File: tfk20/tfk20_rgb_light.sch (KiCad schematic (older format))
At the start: 0 parts

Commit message: Continue on tfk20
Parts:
- added C? (x4): 104, symbol Device:C_Small
- added D? (x4): WS2812B, LED_SMD:LED_WS2812B_PLCC4_5.0x5.0mm_P3.2mm, symbol LED:WS2812B
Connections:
- net RGB_LIGHT: now also D?.4 (DIN)
- new net: D?.2 (DOUT), D?.4 (DIN) (x3)
- new net +5V: C?.1, C?.1, C?.1, C?.1, D?.1 (VDD), D?.1 (VDD), D?.1 (VDD), D?.1 (VDD)
- new net GND: C?.2, C?.2, C?.2, C?.2, D?.3 (VSS), D?.3 (VSS), D?.3 (VSS), D?.3 (VSS)
- no-connect marks 0 -> 2

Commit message: RGB LED driver
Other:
- note added: "RGB underglow LEDs"
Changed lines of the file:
@@
 $Descr A4 11693 8268
 encoding utf-8
-Sheet 4 4
+Sheet 3 4
 Title "tfk20"
 Date "2021-02-02"
@@
 P 2250 1550
 AR Path="/602C3063/601B5D10" Ref="#PWR?"  Part="1"
-AR Path="/602C340B/601B5D10" Ref="#PWR?"  Part="1"
-F 0 "#PWR?" H 2250 1300 50  0001 C CNN
+AR Path="/602C340B/601B5D10" Ref="#PWR0181"  Part="1"
+F 0 "#PWR0181" H 2250 1300 50  0001 C CNN
 F 1 "GND" H 2255 1377 50  0000 C CNN
 F 2 "" H 2250 1550 50  0001 C CNN
@@
 P 1850 1200
 AR Path="/602C3063/601B5D16" Ref="#PWR?"  Part="1"
-AR Path="/602C340B/601B5D16" Ref="#PWR?"  Part="1"
-F 0 "#PWR?" H 1850 1050 50  0001 C CNN
+AR Path="/602C340B/601B5D16" Ref="#PWR0182"  Part="1"
+F 0 "#PWR0182" H 1850 1050 50  0001 C CNN
 F 1 "+5V" H 1865 1373 50  0000 C CNN
 F 2 "" H 1850 1200 50  0001 C CNN
@@
 P 1850 2150
 AR Path="/602C3063/601B5D1E" Ref="#PWR?"  Part="1"
-AR Path="/602C340B/601B5D1E" Ref="#PWR?"  Part="1"
-F 0 "#PWR?" H 1850 1900 50  0001 C CNN
+AR Path="/602C340B/601B5D1E" Ref="#PWR0183"  Part="1"
+F 0 "#PWR0183" H 1850 1900 50  0001 C CNN
 F 1 "GND" H 1855 1977 50  0000 C CNN
 F 2 "" H 1850 2150 50  0001 C CNN
@@
 P 3600 1500
 AR Path="/602C3063/601B5D32" Ref="#PWR?"  Part="1"
-AR Path="/602C340B/601B5D32" Ref="#PWR?"  Part="1"
-F 0 "#PWR?" H 3600 1250 50  0001 C CNN
+AR Path="/602C340B/601B5D32" Ref="#PWR0184"  Part="1"
+F 0 "#PWR0184" H 3600 1250 50  0001 C CNN
 F 1 "GND" H 3605 1327 50  0000 C CNN
 F 2 "" H 3600 1500 50  0001 C CNN
@@
 P 3150 1200
 AR Path="/602C3063/601B5D38" Ref="#PWR?"  Part="1"
-AR Path="/602C340B/601B5D38" Ref="#PWR?"  Part="1"
-F 0 "#PWR?" H 3150 1050 50  0001 C CNN
+AR Path="/602C340B/601B5D38" Ref="#PWR0185"  Part="1"
+F 0 "#PWR0185" H 3150 1050 50  0001 C CNN
 F 1 "+5V" H 3165 1373 50  0000 C CNN
 F 2 "" H 3150 1200 50  0001 C CNN
@@
 P 3150 2150
 AR Path="/602C3063/601B5D40" Ref="#PWR?"  Part="1"
-AR Path="/602C340B/601B5D40" Ref="#PWR?"  Part="1"
-F 0 "#PWR?" H 3150 1900 50  0001 C CNN
+AR Path="/602C340B/601B5D40" Ref="#PWR0186"  Part="1"
+F 0 "#PWR0186" H 3150 1900 50  0001 C CNN
 F 1 "GND" H 3155 1977 50  0000 C CNN
 F 2 "" H 3150 2150 50  0001 C CNN
@@
 P 4850 1550
 AR Path="/602C3063/601B5D55" Ref="#PWR?"  Part="1"
-AR Path="/602C340B/601B5D55" Ref="#PWR?"  Part="1"
-F 0 "#PWR?" H 4850 1300 50  0001 C CNN
+AR Path="/602C340B/601B5D55" Ref="#PWR0187"  Part="1"
+F 0 "#PWR0187" H 4850 1300 50  0001 C CNN
 F 1 "GND" H 4855 1377 50  0000 C CNN
 F 2 "" H 4850 1550 50  0001 C CNN
@@
 P 4450 1200
 AR Path="/602C3063/601B5D5B" Ref="#PWR?"  Part="1"
-AR Path="/602C340B/601B5D5B" Ref="#PWR?"  Part="1"
-F 0 "#PWR?" H 4450 1050 50  0001 C CNN
+AR Path="/602C340B/601B5D5B" Ref="#PWR0188"  Part="1"
+F 0 "#PWR0188" H 4450 1050 50  0001 C CNN
 F 1 "+5V" H 4465 1373 50  0000 C CNN
 F 2 "" H 4450 1200 50  0001 C CNN
@@
 P 4450 2150
 AR Path="/602C3063/601B5D63" Ref="#PWR?"  Part="1"
-AR Path="/602C340B/601B5D63" Ref="#PWR?"  Part="1"
-F 0 "#PWR?" H 4450 1900 50  0001 C CNN
+AR Path="/602C340B/601B5D63" Ref="#PWR0189"  Part="1"
+F 0 "#PWR0189" H 4450 1900 50  0001 C CNN
 F 1 "GND" H 4455 1977 50  0000 C CNN
 F 2 "" H 4450 2150 50  0001 C CNN
@@
 P 6200 1500
 AR Path="/602C3063/601B5D77" Ref="#PWR?"  Part="1"
-AR Path="/602C340B/601B5D77" Ref="#PWR?"  Part="1"
-F 0 "#PWR?" H 6200 1250 50  0001 C CNN
+AR Path="/602C340B/601B5D77" Ref="#PWR0190"  Part="1"
+F 0 "#PWR0190" H 6200 1250 50  0001 C CNN
 F 1 "GND" H 6205 1327 50  0000 C CNN
 F 2 "" H 6200 1500 50  0001 C CNN
@@
 P 5750 1200
 AR Path="/602C3063/601B5D7D" Ref="#PWR?"  Part="1"
-AR Path="/602C340B/601B5D7D" Ref="#PWR?"  Part="1"
-F 0 "#PWR?" H 5750 1050 50  0001 C CNN
+AR Path="/602C340B/601B5D7D" Ref="#PWR0191"  Part="1"
+F 0 "#PWR0191" H 5750 1050 50  0001 C CNN
 F 1 "+5V" H 5765 1373 50  0000 C CNN
 F 2 "" H 5750 1200 50  0001 C CNN
@@
 P 5750 2150
 AR Path="/602C3063/601B5D85" Ref="#PWR?"  Part="1"
-AR Path="/602C340B/601B5D85" Ref="#PWR?"  Part="1"
-F 0 "#PWR?" H 5750 1900 50  0001 C CNN
+AR Path="/602C340B/601B5D85" Ref="#PWR0192"  Part="1"
+F 0 "#PWR0192" H 5750 1900 50  0001 C CNN
 F 1 "GND" H 5755 1977 50  0000 C CNN
 F 2 "" H 5750 2150 50  0001 C CNN
@@
 NoConn ~ 6100 1850
 NoConn ~ -2800 -100
+Text Notes 750  850  0    50   ~ 0
+RGB underglow LEDs
+Wire Notes Line
+	700  700  6650 700
+Wire Notes Line
+	6650 700  6650 2500
+Wire Notes Line
+	6650 2500 700  2500
+Wire Notes Line
+	700  2500 700  700
 $EndSCHEMATC

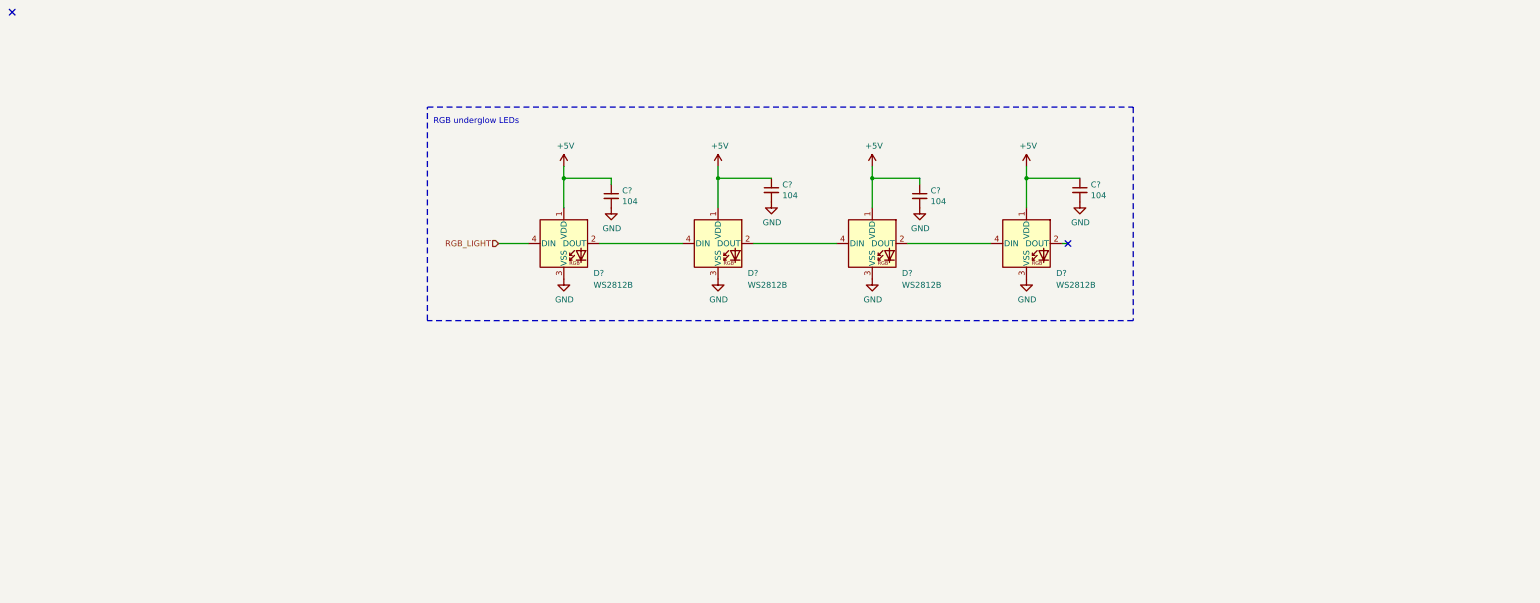
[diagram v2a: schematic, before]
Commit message: Change MCU, add another row, add reset button
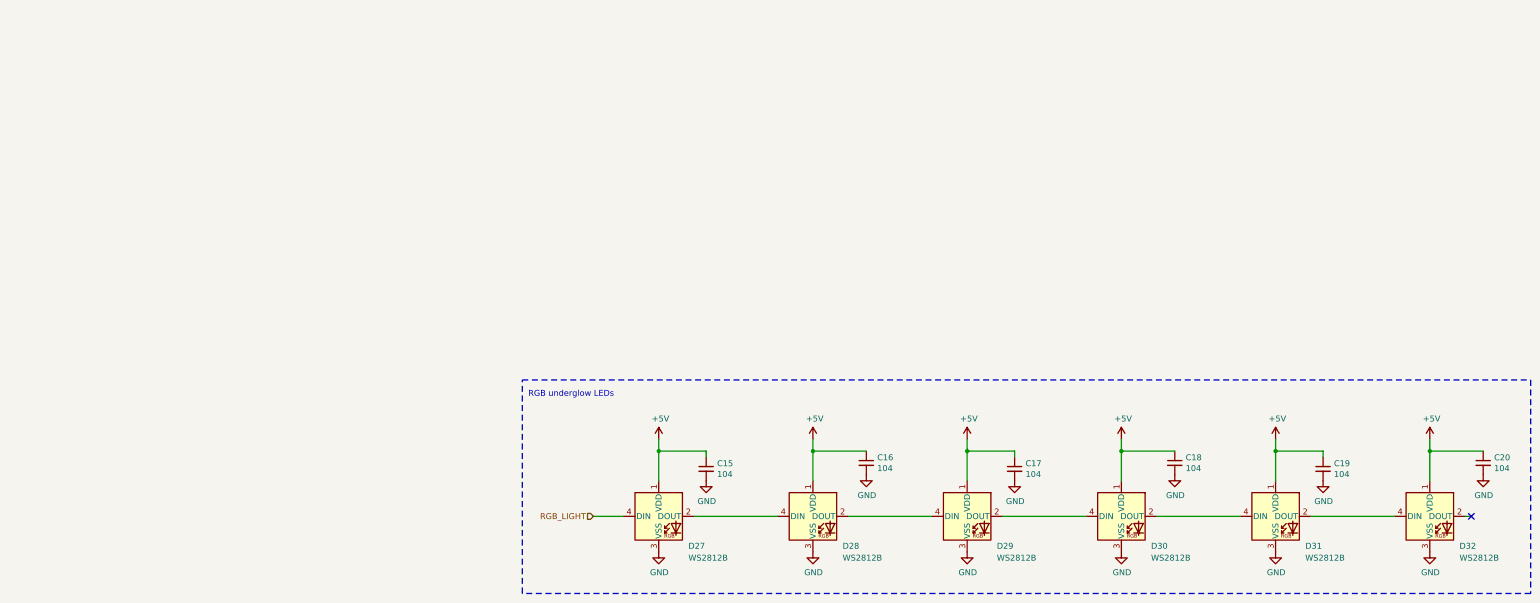
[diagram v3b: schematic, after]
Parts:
- added C19, C20: 104, symbol Device:C_Small
- added D31, D32: WS2812B, LED_SMD:LED_WS2812B_PLCC4_5.0x5.0mm_P3.2mm, symbol LED:WS2812B
- gave numbers to parts that had none: 8
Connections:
- net +5V: now also C19.1, C20.1, D31.1 (VDD), D32.1 (VDD)
- net GND: now also C19.2, C20.2, D31.3 (VSS), D32.3 (VSS)
- net at D30.2 (DOUT): now also D31.4 (DIN)
- new net: D31.2 (DOUT), D32.4 (DIN)
- no-connect marks 2 -> 1
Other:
- moved on the sheet: C15, C16, C17, C18, D27, D28, D29, D30

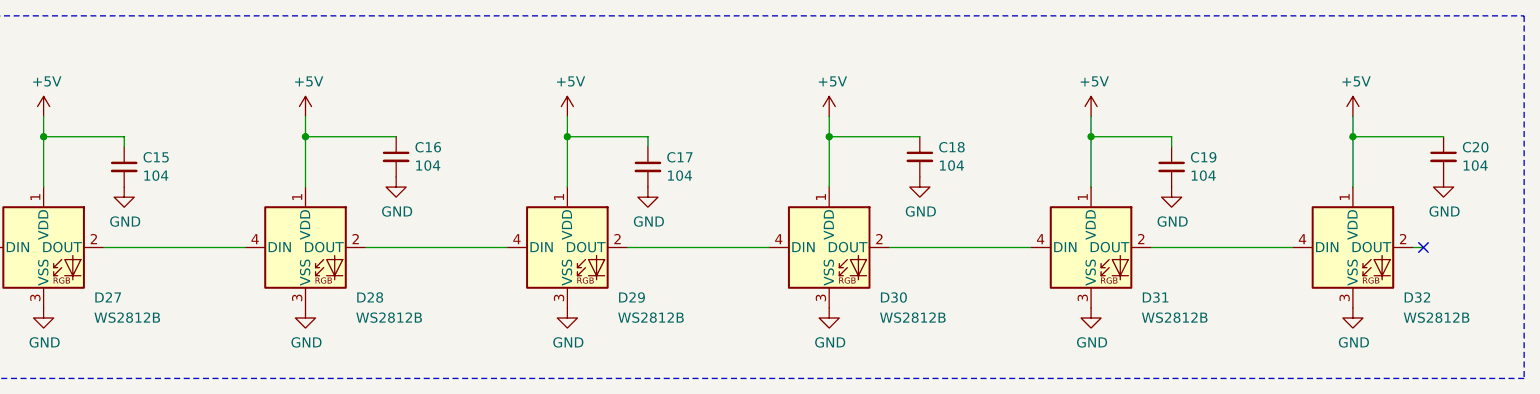
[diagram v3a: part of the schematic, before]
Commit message: Implement sophisticated USB-C protection
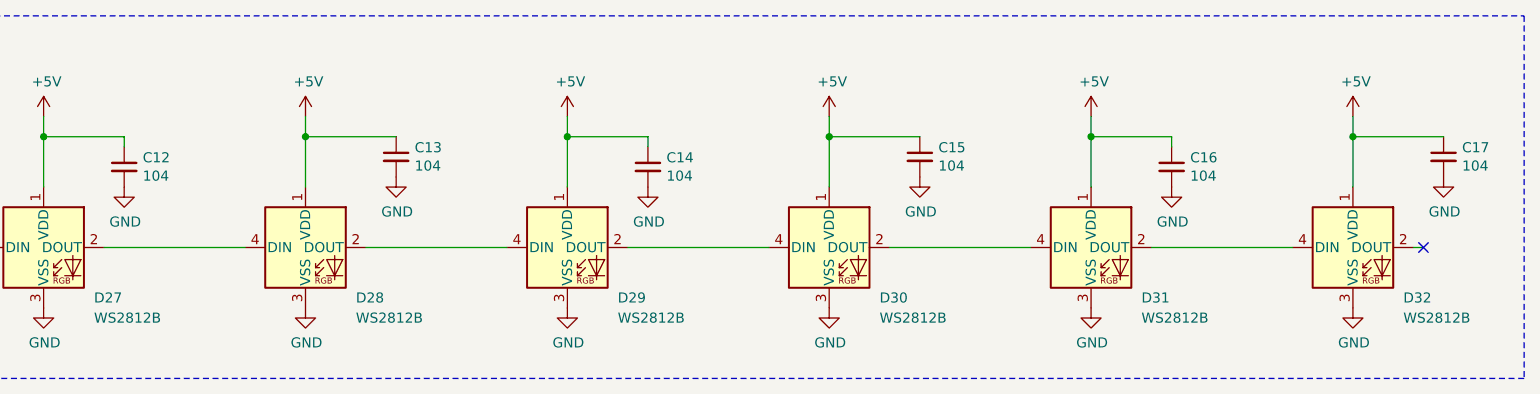
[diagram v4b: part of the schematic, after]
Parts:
- renumbered C15 to C12, C16 to C13, C17 to C14, C18 to C15, C19 to C16, C20 to C17
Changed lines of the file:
@@
 $Descr A4 11693 8268
 encoding utf-8
-Sheet 3 4
+Sheet 3 5
 Title "tfk20"
 Date "2021-02-02"
@@
 P 3050 3750
 AR Path="/602C3063/601B5D07" Ref="C?"  Part="1"
-AR Path="/602C340B/601B5D07" Ref="C15"  Part="1"
-F 0 "C15" H 3142 3796 50  0000 L CNN
+AR Path="/602C340B/601B5D07" Ref="C12"  Part="1"
+F 0 "C12" H 3142 3796 50  0000 L CNN
 F 1 "104" H 3142 3705 50  0000 L CNN
 F 2 "" H 3050 3750 50  0001 C CNN
@@
 P 3050 3850
 AR Path="/602C3063/601B5D10" Ref="#PWR?"  Part="1"
-AR Path="/602C340B/601B5D10" Ref="#PWR034"  Part="1"
-F 0 "#PWR034" H 3050 3600 50  0001 C CNN
+AR Path="/602C340B/601B5D10" Ref="#PWR022"  Part="1"
+F 0 "#PWR022" H 3050 3600 50  0001 C CNN
 F 1 "GND" H 3055 3677 50  0000 C CNN
 F 2 "" H 3050 3850 50  0001 C CNN
@@
 P 2650 3500
 AR Path="/602C3063/601B5D16" Ref="#PWR?"  Part="1"
-AR Path="/602C340B/601B5D16" Ref="#PWR032"  Part="1"
-F 0 "#PWR032" H 2650 3350 50  0001 C CNN
+AR Path="/602C340B/601B5D16" Ref="#PWR020"  Part="1"
+F 0 "#PWR020" H 2650 3350 50  0001 C CNN
 F 1 "+5V" H 2665 3673 50  0000 C CNN
 F 2 "" H 2650 3500 50  0001 C CNN
@@
 P 4400 3700
 AR Path="/602C3063/601B5D2A" Ref="C?"  Part="1"
-AR Path="/602C340B/601B5D2A" Ref="C16"  Part="1"
-F 0 "C16" H 4492 3746 50  0000 L CNN
+AR Path="/602C340B/601B5D2A" Ref="C13"  Part="1"
+F 0 "C13" H 4492 3746 50  0000 L CNN
 F 1 "104" H 4492 3655 50  0000 L CNN
 F 2 "" H 4400 3700 50  0001 C CNN
@@
 P 4400 3800
 AR Path="/602C3063/601B5D32" Ref="#PWR?"  Part="1"
-AR Path="/602C340B/601B5D32" Ref="#PWR037"  Part="1"
-F 0 "#PWR037" H 4400 3550 50  0001 C CNN
+AR Path="/602C340B/601B5D32" Ref="#PWR025"  Part="1"
+F 0 "#PWR025" H 4400 3550 50  0001 C CNN
 F 1 "GND" H 4405 3627 50  0000 C CNN
 F 2 "" H 4400 3800 50  0001 C CNN
@@
 P 3950 3500
 AR Path="/602C3063/601B5D38" Ref="#PWR?"  Part="1"
-AR Path="/602C340B/601B5D38" Ref="#PWR035"  Part="1"
-F 0 "#PWR035" H 3950 3350 50  0001 C CNN
+AR Path="/602C340B/601B5D38" Ref="#PWR023"  Part="1"
+F 0 "#PWR023" H 3950 3350 50  0001 C CNN
 F 1 "+5V" H 3965 3673 50  0000 C CNN
 F 2 "" H 3950 3500 50  0001 C CNN
@@
 P 3950 4450
 AR Path="/602C3063/601B5D40" Ref="#PWR?"  Part="1"
-AR Path="/602C340B/601B5D40" Ref="#PWR036"  Part="1"
-F 0 "#PWR036" H 3950 4200 50  0001 C CNN
+AR Path="/602C340B/601B5D40" Ref="#PWR024"  Part="1"
+F 0 "#PWR024" H 3950 4200 50  0001 C CNN
 F 1 "GND" H 3955 4277 50  0000 C CNN
 F 2 "" H 3950 4450 50  0001 C CNN
@@
 P 5650 3750
 AR Path="/602C3063/601B5D4C" Ref="C?"  Part="1"
-AR Path="/602C340B/601B5D4C" Ref="C17"  Part="1"
-F 0 "C17" H 5742 3796 50  0000 L CNN
+AR Path="/602C340B/601B5D4C" Ref="C14"  Part="1"
+F 0 "C14" H 5742 3796 50  0000 L CNN
 F 1 "104" H 5742 3705 50  0000 L CNN
 F 2 "" H 5650 3750 50  0001 C CNN
@@
 P 5650 3850
 AR Path="/602C3063/601B5D55" Ref="#PWR?"  Part="1"
-AR Path="/602C340B/601B5D55" Ref="#PWR040"  Part="1"
-F 0 "#PWR040" H 5650 3600 50  0001 C CNN
+AR Path="/602C340B/601B5D55" Ref="#PWR028"  Part="1"
+F 0 "#PWR028" H 5650 3600 50  0001 C CNN
 F 1 "GND" H 5655 3677 50  0000 C CNN
 F 2 "" H 5650 3850 50  0001 C CNN
@@
 P 5250 3500
 AR Path="/602C3063/601B5D5B" Ref="#PWR?"  Part="1"
-AR Path="/602C340B/601B5D5B" Ref="#PWR038"  Part="1"
-F 0 "#PWR038" H 5250 3350 50  0001 C CNN
+AR Path="/602C340B/601B5D5B" Ref="#PWR026"  Part="1"
+F 0 "#PWR026" H 5250 3350 50  0001 C CNN
 F 1 "+5V" H 5265 3673 50  0000 C CNN
 F 2 "" H 5250 3500 50  0001 C CNN
@@
 P 5250 4450
 AR Path="/602C3063/601B5D63" Ref="#PWR?"  Part="1"
-AR Path="/602C340B/601B5D63" Ref="#PWR039"  Part="1"
-F 0 "#PWR039" H 5250 4200 50  0001 C CNN
+AR Path="/602C340B/601B5D63" Ref="#PWR027"  Part="1"
+F 0 "#PWR027" H 5250 4200 50  0001 C CNN
 F 1 "GND" H 5255 4277 50  0000 C CNN
 F 2 "" H 5250 4450 50  0001 C CNN
@@
 P 7000 3700
 AR Path="/602C3063/601B5D6F" Ref="C?"  Part="1"
-AR Path="/602C340B/601B5D6F" Ref="C18"  Part="1"
-F 0 "C18" H 7092 3746 50  0000 L CNN
+AR Path="/602C340B/601B5D6F" Ref="C15"  Part="1"
+F 0 "C15" H 7092 3746 50  0000 L CNN
 F 1 "104" H 7092 3655 50  0000 L CNN
 F 2 "" H 7000 3700 50  0001 C CNN
@@
 P 7000 3800
 AR Path="/602C3063/601B5D77" Ref="#PWR?"  Part="1"
-AR Path="/602C340B/601B5D77" Ref="#PWR043"  Part="1"
-F 0 "#PWR043" H 7000 3550 50  0001 C CNN
+AR Path="/602C340B/601B5D77" Ref="#PWR031"  Part="1"
+F 0 "#PWR031" H 7000 3550 50  0001 C CNN
 F 1 "GND" H 7005 3627 50  0000 C CNN
 F 2 "" H 7000 3800 50  0001 C CNN
@@
 P 6550 3500
 AR Path="/602C3063/601B5D7D" Ref="#PWR?"  Part="1"
-AR Path="/602C340B/601B5D7D" Ref="#PWR041"  Part="1"
-F 0 "#PWR041" H 6550 3350 50  0001 C CNN
+AR Path="/602C340B/601B5D7D" Ref="#PWR029"  Part="1"
+F 0 "#PWR029" H 6550 3350 50  0001 C CNN
 F 1 "+5V" H 6565 3673 50  0000 C CNN
 F 2 "" H 6550 3500 50  0001 C CNN
@@
 P 6550 4450
 AR Path="/602C3063/601B5D85" Ref="#PWR?"  Part="1"
-AR Path="/602C340B/601B5D85" Ref="#PWR042"  Part="1"
-F 0 "#PWR042" H 6550 4200 50  0001 C CNN
+AR Path="/602C340B/601B5D85" Ref="#PWR030"  Part="1"
+F 0 "#PWR030" H 6550 4200 50  0001 C CNN
 F 1 "GND" H 6555 4277 50  0000 C CNN
 F 2 "" H 6550 4450 50  0001 C CNN
@@
 	1500 4800 1500 3000
 $Comp
-L power:GND #PWR033
+L power:GND #PWR021
 U 1 1 606DE53F
 P 2650 4450
-F 0 "#PWR033" H 2650 4200 50  0001 C CNN
+F 0 "#PWR021" H 2650 4200 50  0001 C CNN
 F 1 "GND" H 2655 4277 50  0000 C CNN
 F 2 "" H 2650 4450 50  0001 C CNN
@@
 P 8250 3750
 AR Path="/602C3063/60DF2224" Ref="C?"  Part="1"
-AR Path="/602C340B/60DF2224" Ref="C19"  Part="1"
-F 0 "C19" H 8342 3796 50  0000 L CNN
+AR Path="/602C340B/60DF2224" Ref="C16"  Part="1"
+F 0 "C16" H 8342 3796 50  0000 L CNN
 F 1 "104" H 8342 3705 50  0000 L CNN
 F 2 "" H 8250 3750 50  0001 C CNN
@@
 P 8250 3850
 AR Path="/602C3063/60DF222D" Ref="#PWR?"  Part="1"
-AR Path="/602C340B/60DF222D" Ref="#PWR046"  Part="1"
-F 0 "#PWR046" H 8250 3600 50  0001 C CNN
+AR Path="/602C340B/60DF222D" Ref="#PWR034"  Part="1"
+F 0 "#PWR034" H 8250 3600 50  0001 C CNN
 F 1 "GND" H 8255 3677 50  0000 C CNN
 F 2 "" H 8250 3850 50  0001 C CNN
@@
 P 7850 3500
 AR Path="/602C3063/60DF2233" Ref="#PWR?"  Part="1"
-AR Path="/602C340B/60DF2233" Ref="#PWR044"  Part="1"
-F 0 "#PWR044" H 7850 3350 50  0001 C CNN
+AR Path="/602C340B/60DF2233" Ref="#PWR032"  Part="1"
+F 0 "#PWR032" H 7850 3350 50  0001 C CNN
 F 1 "+5V" H 7865 3673 50  0000 C CNN
 F 2 "" H 7850 3500 50  0001 C CNN
@@
 P 7850 4450
 AR Path="/602C3063/60DF223B" Ref="#PWR?"  Part="1"
-AR Path="/602C340B/60DF223B" Ref="#PWR045"  Part="1"
-F 0 "#PWR045" H 7850 4200 50  0001 C CNN
+AR Path="/602C340B/60DF223B" Ref="#PWR033"  Part="1"
+F 0 "#PWR033" H 7850 4200 50  0001 C CNN
 F 1 "GND" H 7855 4277 50  0000 C CNN
 F 2 "" H 7850 4450 50  0001 C CNN
@@
 P 9600 3700
 AR Path="/602C3063/60DF2247" Ref="C?"  Part="1"
-AR Path="/602C340B/60DF2247" Ref="C20"  Part="1"
-F 0 "C20" H 9692 3746 50  0000 L CNN
+AR Path="/602C340B/60DF2247" Ref="C17"  Part="1"
+F 0 "C17" H 9692 3746 50  0000 L CNN
 F 1 "104" H 9692 3655 50  0000 L CNN
 F 2 "" H 9600 3700 50  0001 C CNN
@@
 P 9600 3800
 AR Path="/602C3063/60DF224F" Ref="#PWR?"  Part="1"
-AR Path="/602C340B/60DF224F" Ref="#PWR049"  Part="1"
-F 0 "#PWR049" H 9600 3550 50  0001 C CNN
+AR Path="/602C340B/60DF224F" Ref="#PWR037"  Part="1"
+F 0 "#PWR037" H 9600 3550 50  0001 C CNN
 F 1 "GND" H 9605 3627 50  0000 C CNN
 F 2 "" H 9600 3800 50  0001 C CNN
@@
 P 9150 3500
 AR Path="/602C3063/60DF2255" Ref="#PWR?"  Part="1"
-AR Path="/602C340B/60DF2255" Ref="#PWR047"  Part="1"
-F 0 "#PWR047" H 9150 3350 50  0001 C CNN
+AR Path="/602C340B/60DF2255" Ref="#PWR035"  Part="1"
+F 0 "#PWR035" H 9150 3350 50  0001 C CNN
 F 1 "+5V" H 9165 3673 50  0000 C CNN
 F 2 "" H 9150 3500 50  0001 C CNN
@@
 P 9150 4450
 AR Path="/602C3063/60DF225D" Ref="#PWR?"  Part="1"
-AR Path="/602C340B/60DF225D" Ref="#PWR048"  Part="1"
-F 0 "#PWR048" H 9150 4200 50  0001 C CNN
+AR Path="/602C340B/60DF225D" Ref="#PWR036"  Part="1"
+F 0 "#PWR036" H 9150 4200 50  0001 C CNN
 F 1 "GND" H 9155 4277 50  0000 C CNN
 F 2 "" H 9150 4450 50  0001 C CNN

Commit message: Add STL11N3LLH6 footprint
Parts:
- renumbered C12 to C301, C13 to C302, C14 to C303, C15 to C304, C16 to C305, C17 to C306, D27 to D301, D28 to D302, D29 to D303, D30 to D304, D31 to D305, D32 to D306
